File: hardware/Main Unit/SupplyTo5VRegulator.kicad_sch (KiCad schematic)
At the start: 22 parts, among them U14 TPS56A37RPAR, U17 INA180A3

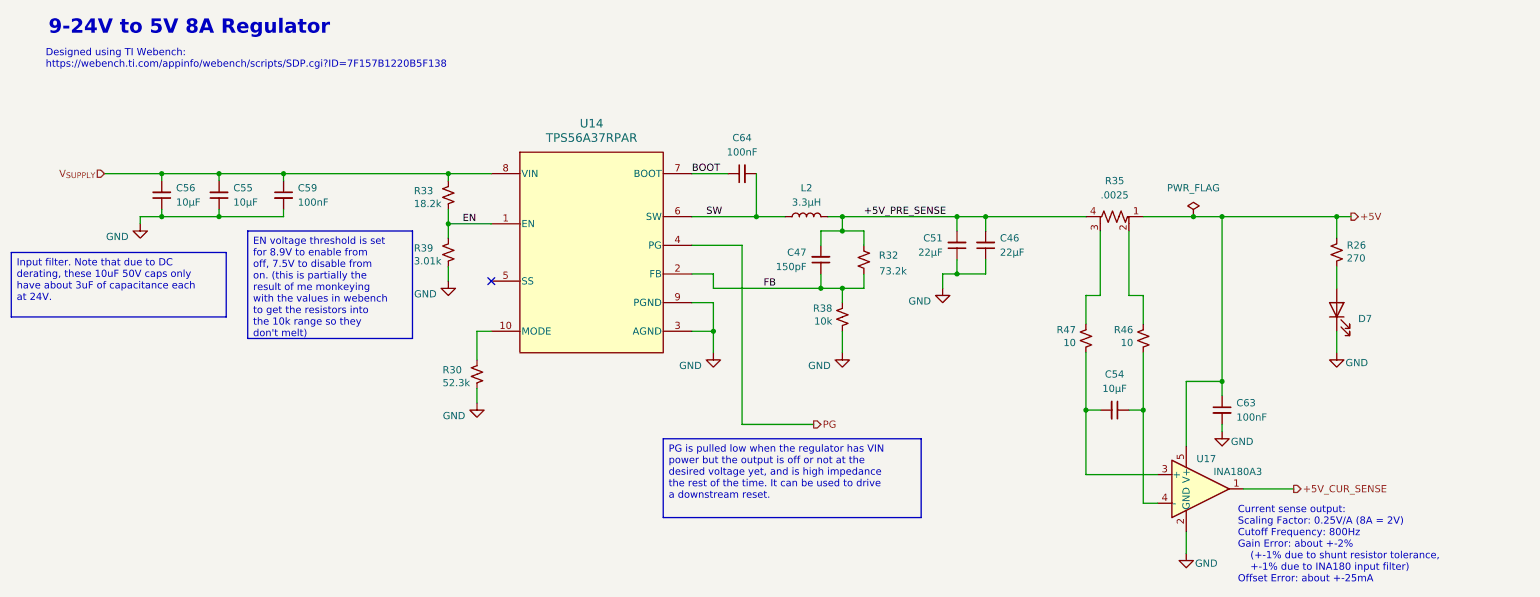
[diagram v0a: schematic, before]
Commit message: Update main unit to KiCAD 10, add clock buffer
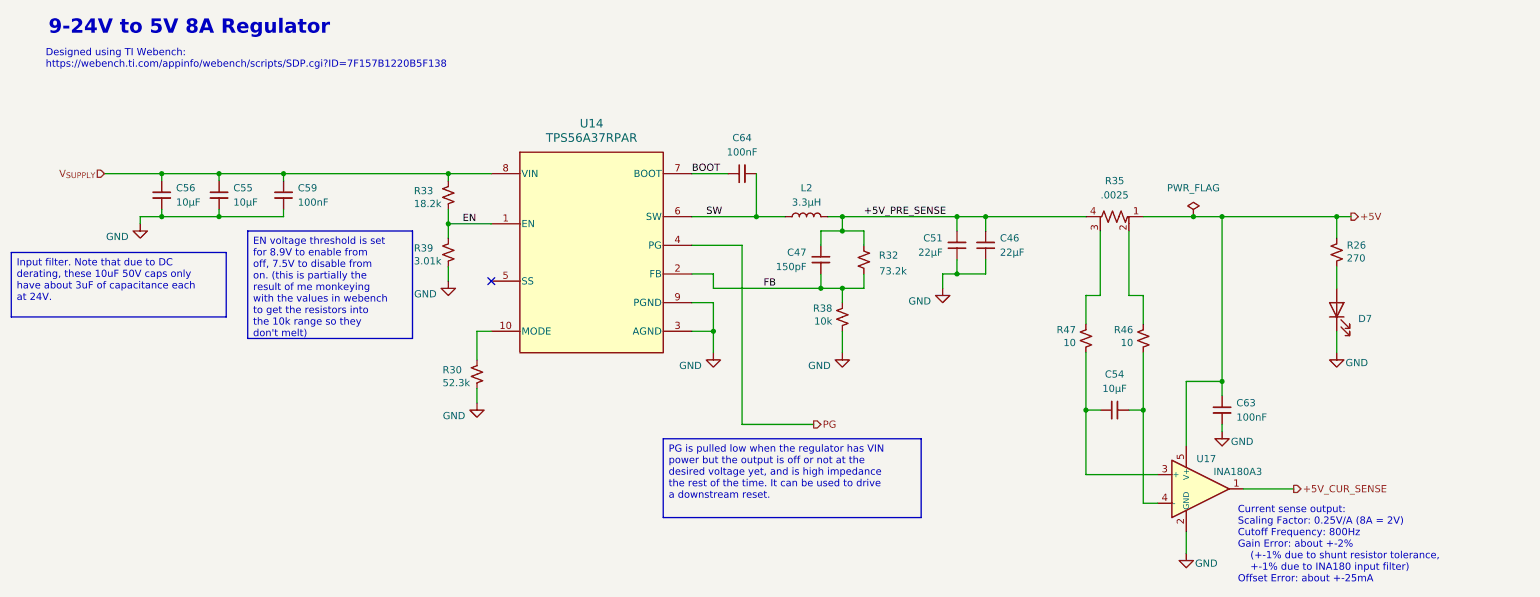
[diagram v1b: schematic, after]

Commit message: Oops forgot to save
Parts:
- C48: renamed from C46; KiLib_Generator (none) -> Digi-Key
- C49: renamed from C47; KiLib_Generator (none) -> Digi-Key
- C53: renamed from C51; KiLib_Generator (none) -> Digi-Key
- C56: renamed from C55; KiLib_Generator (none) -> Digi-Key
- C57: renamed from C56; KiLib_Generator (none) -> Digi-Key
- C58: renamed from C54; KiLib_Generator (none) -> Digi-Key
- C59, R26, R30, R32, R33, R46, R47: KiLib_Generator (none) -> Digi-Key
- C65: renamed from C63; KiLib_Generator (none) -> Digi-Key
- C66: renamed from C64; KiLib_Generator (none) -> Digi-Key
- L2: KiLib_Generator (none) -> 541-1352-1-ND
- R37: renamed from R38; KiLib_Generator (none) -> Digi-Key
- R38: renamed from R39; KiLib_Generator (none) -> Digi-Key
- U19: renamed from U17; KiLib_Generator (none) -> Digi-Key
- renumbered R35 to R34, U14 to U16
